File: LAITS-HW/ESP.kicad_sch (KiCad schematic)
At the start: 52 parts, among them J501 JTAG, SW501 SW_BOOT, SW502 SW_RST, SW503 SW_LOG_SD_EN, SW504 SW_RST_PROV, SW505 SW_RGB_EN, SW506 SW_SLEEP, U501 ESP32-WROVER-IE/E, U502 SX1503I091TRT

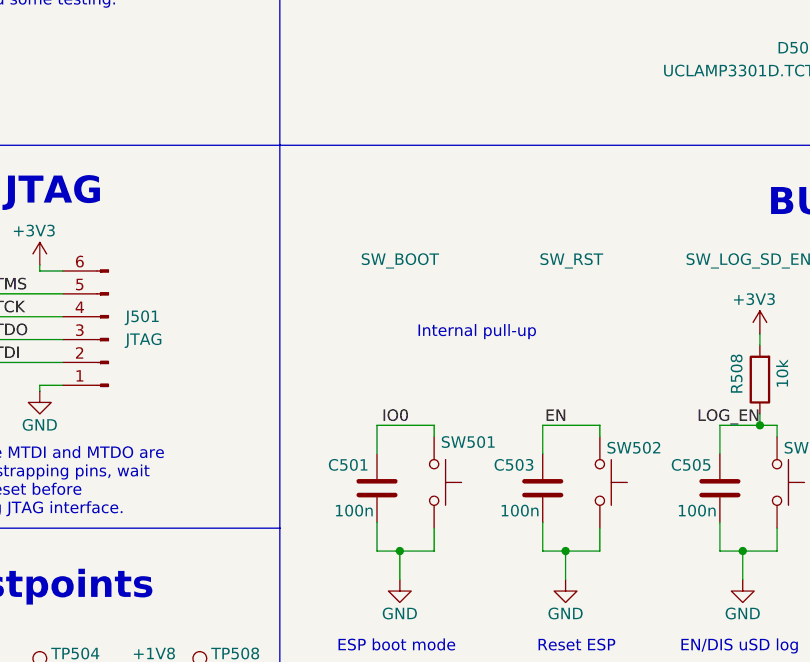
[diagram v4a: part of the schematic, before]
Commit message: Marked C501 as DNP to ensure proper startup sequence
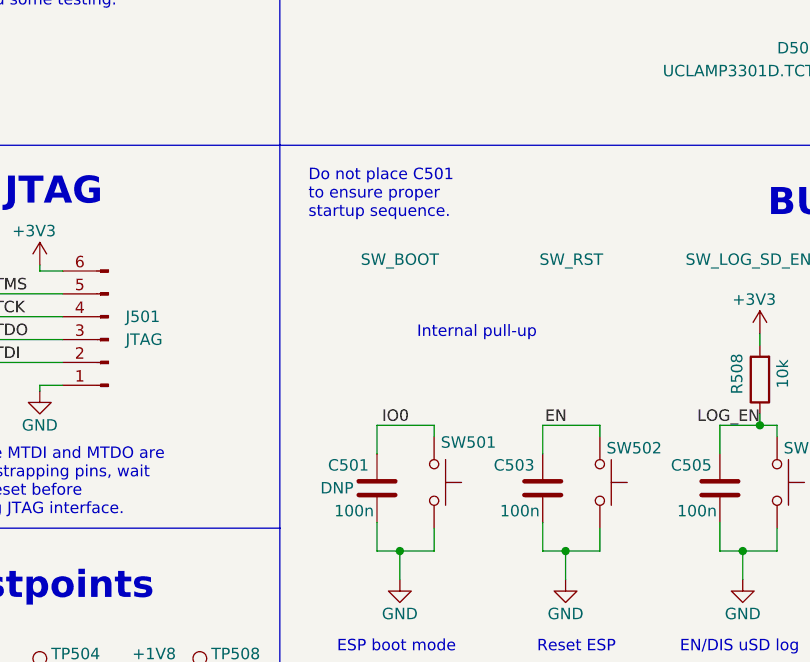
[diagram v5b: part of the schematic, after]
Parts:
- C501: Place (none) -> DNP; now left out of the parts list
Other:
- note added: "Do not place C501 to ensure proper startup sequence."
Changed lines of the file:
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@@
+    (effects (font (size 1.27 1.27)) (justify left bottom))
+  )
+  (text "Do not place C501\nto ensure proper\nstartup sequence."
+    (at 66.04 110.49 0)
     (effects (font (size 1.27 1.27)) (justify left bottom))
   )
@@
   )
   (symbol (lib_id "Device:C") (at 73.66 140.335 180) (unit 1)
-    (in_bom yes) (on_board yes)
+    (in_bom no) (on_board yes)
     (property "Reference" "C501" (id 0) (at 70.485 137.795 0))
     (property "Value" "100n" (id 1) (at 71.12 142.875 0))
@@
       (effects (font (size 1.27 1.27)) hide)
     )
-    (pin "1")
-    (pin "2")
+    (property "Place" "DNP" (id 4) (at 69.215 140.335 0))
+    (pin "1")
+    (pin "2")

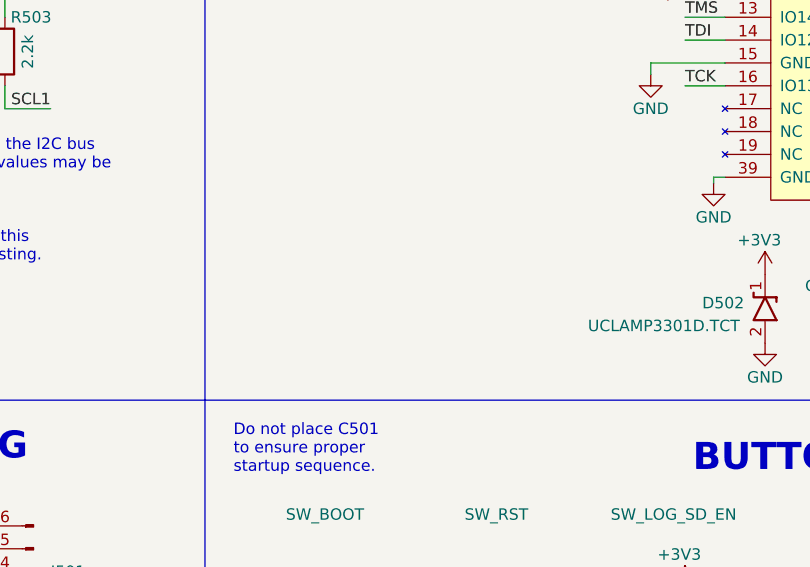
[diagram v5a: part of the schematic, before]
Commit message: Add small info about ESP antenna selector on schematic
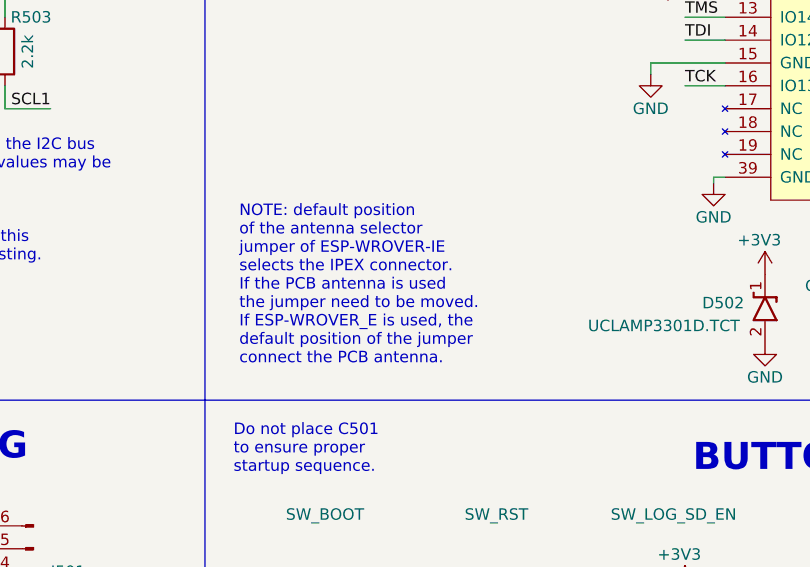
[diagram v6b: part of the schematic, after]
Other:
- note added: "NOTE: default position of the antenna selector jumper of ESP-WROVER-IE selects the IPEX connector. If the PCB antenna is used the jumper need to be moved. If ESP-WROVER_E is used, the default position of the jumper connect the PCB antenna."
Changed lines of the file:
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@@
+    (effects (font (size 1.27 1.27)) (justify left bottom))
+  )
+  (text "NOTE: default position\nof the antenna selector\njumper of ESP-WROVER-IE\nselects the IPEX connector.\nIf the PCB antenna is used\nthe jumper need to be moved.\nIf ESP-WROVER_E is used, the\ndefault position of the jumper\nconnect the PCB antenna."
+    (at 66.675 98.425 0)
     (effects (font (size 1.27 1.27)) (justify left bottom))
   )
